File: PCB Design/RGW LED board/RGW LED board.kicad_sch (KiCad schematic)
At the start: 13 parts

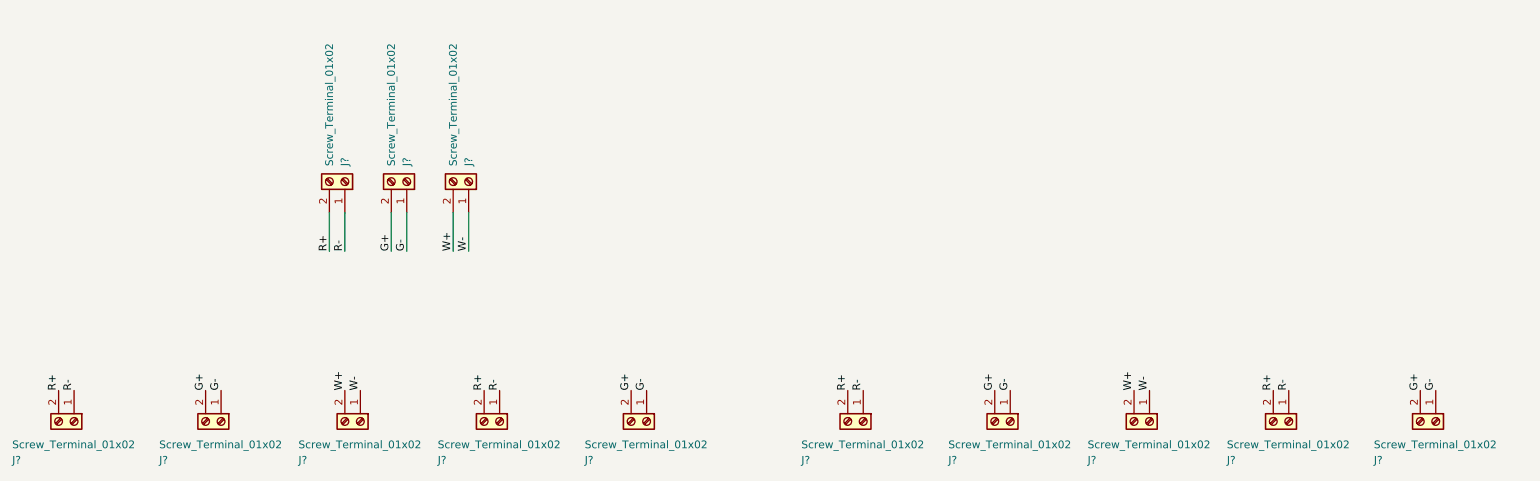
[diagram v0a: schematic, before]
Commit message: schematic now has no errors
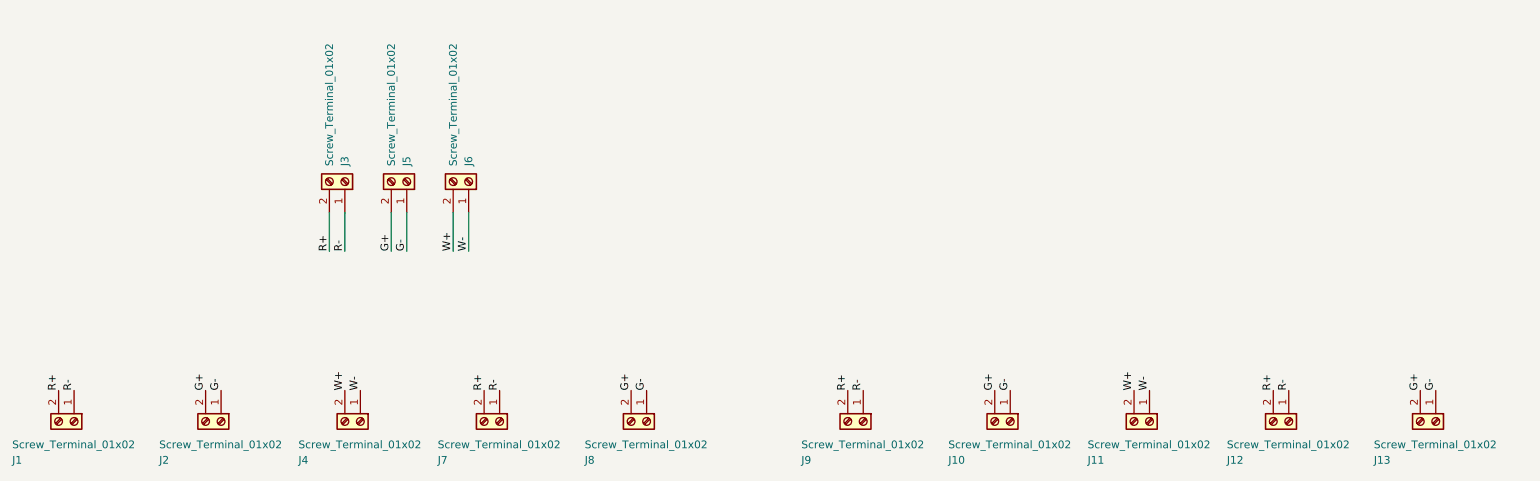
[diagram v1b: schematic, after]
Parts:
- gave numbers to parts that had none: 13
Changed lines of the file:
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@@
   (symbol (lib_id "Connector:Screw_Terminal_01x02") (at 69.85 100.33 270) (unit 1)
     (in_bom yes) (on_board yes)
-    (property "Reference" "J?" (id 0) (at 59.69 106.68 90)
+    (property "Reference" "J2" (id 0) (at 59.69 106.68 90)
       (effects (font (size 1.27 1.27)) (justify left))
     )
@@
   (symbol (lib_id "Connector:Screw_Terminal_01x02") (at 90.17 60.96 270) (mirror x) (unit 1)
     (in_bom yes) (on_board yes) (fields_autoplaced)
-    (property "Reference" "J?" (id 0) (at 90.1701 58.42 0)
+    (property "Reference" "J3" (id 0) (at 90.1701 58.42 0)
       (effects (font (size 1.27 1.27)) (justify left))
     )
@@
   (symbol (lib_id "Connector:Screw_Terminal_01x02") (at 245.11 100.33 270) (unit 1)
     (in_bom yes) (on_board yes)
-    (property "Reference" "J?" (id 0) (at 234.95 106.68 90)
+    (property "Reference" "J12" (id 0) (at 234.95 106.68 90)
       (effects (font (size 1.27 1.27)) (justify left))
     )
@@
   (symbol (lib_id "Connector:Screw_Terminal_01x02") (at 199.39 100.33 270) (unit 1)
     (in_bom yes) (on_board yes)
-    (property "Reference" "J?" (id 0) (at 189.23 106.68 90)
+    (property "Reference" "J10" (id 0) (at 189.23 106.68 90)
       (effects (font (size 1.27 1.27)) (justify left))
     )
@@
   (symbol (lib_id "Connector:Screw_Terminal_01x02") (at 45.72 100.33 270) (unit 1)
     (in_bom yes) (on_board yes)
-    (property "Reference" "J?" (id 0) (at 35.56 106.68 90)
+    (property "Reference" "J1" (id 0) (at 35.56 106.68 90)
       (effects (font (size 1.27 1.27)) (justify left))
     )
@@
   (symbol (lib_id "Connector:Screw_Terminal_01x02") (at 222.25 100.33 270) (unit 1)
     (in_bom yes) (on_board yes)
-    (property "Reference" "J?" (id 0) (at 212.09 106.68 90)
+    (property "Reference" "J11" (id 0) (at 212.09 106.68 90)
       (effects (font (size 1.27 1.27)) (justify left))
     )
@@
   (symbol (lib_id "Connector:Screw_Terminal_01x02") (at 115.57 100.33 270) (unit 1)
     (in_bom yes) (on_board yes)
-    (property "Reference" "J?" (id 0) (at 105.41 106.68 90)
+    (property "Reference" "J7" (id 0) (at 105.41 106.68 90)
       (effects (font (size 1.27 1.27)) (justify left))
     )
@@
   (symbol (lib_id "Connector:Screw_Terminal_01x02") (at 139.7 100.33 270) (unit 1)
     (in_bom yes) (on_board yes)
-    (property "Reference" "J?" (id 0) (at 129.54 106.68 90)
+    (property "Reference" "J8" (id 0) (at 129.54 106.68 90)
       (effects (font (size 1.27 1.27)) (justify left))
     )
@@
   (symbol (lib_id "Connector:Screw_Terminal_01x02") (at 100.33 60.96 270) (mirror x) (unit 1)
     (in_bom yes) (on_board yes) (fields_autoplaced)
-    (property "Reference" "J?" (id 0) (at 100.3301 58.42 0)
+    (property "Reference" "J5" (id 0) (at 100.3301 58.42 0)
       (effects (font (size 1.27 1.27)) (justify left))
     )
@@
   (symbol (lib_id "Connector:Screw_Terminal_01x02") (at 110.49 60.96 270) (mirror x) (unit 1)
     (in_bom yes) (on_board yes) (fields_autoplaced)
-    (property "Reference" "J?" (id 0) (at 110.4901 58.42 0)
+    (property "Reference" "J6" (id 0) (at 110.4901 58.42 0)
       (effects (font (size 1.27 1.27)) (justify left))
     )
@@
   (symbol (lib_id "Connector:Screw_Terminal_01x02") (at 175.26 100.33 270) (unit 1)
     (in_bom yes) (on_board yes)
-    (property "Reference" "J?" (id 0) (at 165.1 106.68 90)
+    (property "Reference" "J9" (id 0) (at 165.1 106.68 90)
       (effects (font (size 1.27 1.27)) (justify left))
     )
@@
   (symbol (lib_id "Connector:Screw_Terminal_01x02") (at 92.71 100.33 270) (unit 1)
     (in_bom yes) (on_board yes)
-    (property "Reference" "J?" (id 0) (at 82.55 106.68 90)
+    (property "Reference" "J4" (id 0) (at 82.55 106.68 90)
       (effects (font (size 1.27 1.27)) (justify left))
     )
@@
   (symbol (lib_id "Connector:Screw_Terminal_01x02") (at 269.24 100.33 270) (unit 1)
     (in_bom yes) (on_board yes)
-    (property "Reference" "J?" (id 0) (at 259.08 106.68 90)
+    (property "Reference" "J13" (id 0) (at 259.08 106.68 90)
       (effects (font (size 1.27 1.27)) (justify left))
     )
@@
   )
   (symbol_instances
+    (path "/59271f0a-9961-4fdc-9254-d35e340b8844"
+      (reference "J1") (unit 1) (value "Screw_Terminal_01x02") (footprint "Connector_PinHeader_2.54mm:PinHeader_1x02_P2.54mm_Vertical")
+    )
     (path "/05bc4c2d-ee3e-4b27-9ca2-add16f2c2396"
-      (reference "J?") (unit 1) (value "Screw_Terminal_01x02") (footprint "Connector_PinHeader_2.54mm:PinHeader_1x02_P2.54mm_Vertical")
+      (reference "J2") (unit 1) (value "Screw_Terminal_01x02") (footprint "Connector_PinHeader_2.54mm:PinHeader_1x02_P2.54mm_Vertical")
     )
     (path "/1e7cae58-6b42-419f-a0ef-656c9ebb3a41"
-      (reference "J?") (unit 1) (value "Screw_Terminal_01x02") (footprint "Connector_PinHeader_2.54mm:PinHeader_1x02_P2.54mm_Vertical")
+      (reference "J3") (unit 1) (value "Screw_Terminal_01x02") (footprint "Connector_PinHeader_2.54mm:PinHeader_1x02_P2.54mm_Vertical")
+    )
+    (path "/cdef1967-1f55-4bfe-8dbe-29150df572c3"
+      (reference "J4") (unit 1) (value "Screw_Terminal_01x02") (footprint "Connector_PinHeader_2.54mm:PinHeader_1x02_P2.54mm_Vertical")
+    )
+    (path "/7cca2ccf-cb11-4d5d-9ced-7f6969303b76"
+      (reference "J5") (unit 1) (value "Screw_Terminal_01x02") (footprint "Connector_PinHeader_2.54mm:PinHeader_1x02_P2.54mm_Vertical")
+    )
+    (path "/88f10c66-dda7-46b8-8caf-c98ed0e09c27"
+      (reference "J6") (unit 1) (value "Screw_Terminal_01x02") (footprint "Connector_PinHeader_2.54mm:PinHeader_1x02_P2.54mm_Vertical")
+    )
+    (path "/7aedd637-1cd8-47fd-b299-724180e1fa7b"
+      (reference "J7") (unit 1) (value "Screw_Terminal_01x02") (footprint "Connector_PinHeader_2.54mm:PinHeader_1x02_P2.54mm_Vertical")
+    )
+    (path "/7b3a097c-f841-4a54-8583-32e579f4440f"
+      (reference "J8") (unit 1) (value "Screw_Terminal_01x02") (footprint "Connector_PinHeader_2.54mm:PinHeader_1x02_P2.54mm_Vertical")
+    )
+    (path "/c30a76a9-64f5-4b01-80cf-8af90fc9d1c9"
+      (reference "J9") (unit 1) (value "Screw_Terminal_01x02") (footprint "Connector_PinHeader_2.54mm:PinHeader_1x02_P2.54mm_Vertical")
+    )
+    (path "/2282b147-a81b-4f06-be53-0e383bde0a1a"
+      (reference "J10") (unit 1) (value "Screw_Terminal_01x02") (footprint "Connector_PinHeader_2.54mm:PinHeader_1x02_P2.54mm_Vertical")
+    )
+    (path "/606a80ab-4a3a-4302-a9dd-66db51becec5"
+      (reference "J11") (unit 1) (value "Screw_Terminal_01x02") (footprint "Connector_PinHeader_2.54mm:PinHeader_1x02_P2.54mm_Vertical")
     )
     (path "/205c93a4-41c9-43d8-8f82-bdc6bf726d28"
-      (reference "J?") (unit 1) (value "Screw_Terminal_01x02") (footprint "Connector_PinHeader_2.54mm:PinHeader_1x02_P2.54mm_Vertical")
-    )
-    (path "/2282b147-a81b-4f06-be53-0e383bde0a1a"
-      (reference "J?") (unit 1) (value "Screw_Terminal_01x02") (footprint "Connector_PinHeader_2.54mm:PinHeader_1x02_P2.54mm_Vertical")
-    )
-    (path "/59271f0a-9961-4fdc-9254-d35e340b8844"
-      (reference "J?") (unit 1) (value "Screw_Terminal_01x02") (footprint "Connector_PinHeader_2.54mm:PinHeader_1x02_P2.54mm_Vertical")
-    )
-    (path "/606a80ab-4a3a-4302-a9dd-66db51becec5"
-      (reference "J?") (unit 1) (value "Screw_Terminal_01x02") (footprint "Connector_PinHeader_2.54mm:PinHeader_1x02_P2.54mm_Vertical")
-    )
-    (path "/7aedd637-1cd8-47fd-b299-724180e1fa7b"
-      (reference "J?") (unit 1) (value "Screw_Terminal_01x02") (footprint "Connector_PinHeader_2.54mm:PinHeader_1x02_P2.54mm_Vertical")
-    )
-    (path "/7b3a097c-f841-4a54-8583-32e579f4440f"
-      (reference "J?") (unit 1) (value "Screw_Terminal_01x02") (footprint "Connector_PinHeader_2.54mm:PinHeader_1x02_P2.54mm_Vertical")
-    )
-    (path "/7cca2ccf-cb11-4d5d-9ced-7f6969303b76"
-      (reference "J?") (unit 1) (value "Screw_Terminal_01x02") (footprint "Connector_PinHeader_2.54mm:PinHeader_1x02_P2.54mm_Vertical")
-    )
-    (path "/88f10c66-dda7-46b8-8caf-c98ed0e09c27"
-      (reference "J?") (unit 1) (value "Screw_Terminal_01x02") (footprint "Connector_PinHeader_2.54mm:PinHeader_1x02_P2.54mm_Vertical")
-    )
-    (path "/c30a76a9-64f5-4b01-80cf-8af90fc9d1c9"
-      (reference "J?") (unit 1) (value "Screw_Terminal_01x02") (footprint "Connector_PinHeader_2.54mm:PinHeader_1x02_P2.54mm_Vertical")
-    )
-    (path "/cdef1967-1f55-4bfe-8dbe-29150df572c3"
-      (reference "J?") (unit 1) (value "Screw_Terminal_01x02") (footprint "Connector_PinHeader_2.54mm:PinHeader_1x02_P2.54mm_Vertical")
+      (reference "J12") (unit 1) (value "Screw_Terminal_01x02") (footprint "Connector_PinHeader_2.54mm:PinHeader_1x02_P2.54mm_Vertical")
     )
     (path "/e67ce681-360e-4525-b138-4a854df1c513"
-      (reference "J?") (unit 1) (value "Screw_Terminal_01x02") (footprint "Connector_PinHeader_2.54mm:PinHeader_1x02_P2.54mm_Vertical")
-    )
-  )
+      (reference "J13") (unit 1) (value "Screw_Terminal_01x02") (footprint "Connector_PinHeader_2.54mm:PinHeader_1x02_P2.54mm_Vertical")
+    )
+  )

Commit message: Labeling on components
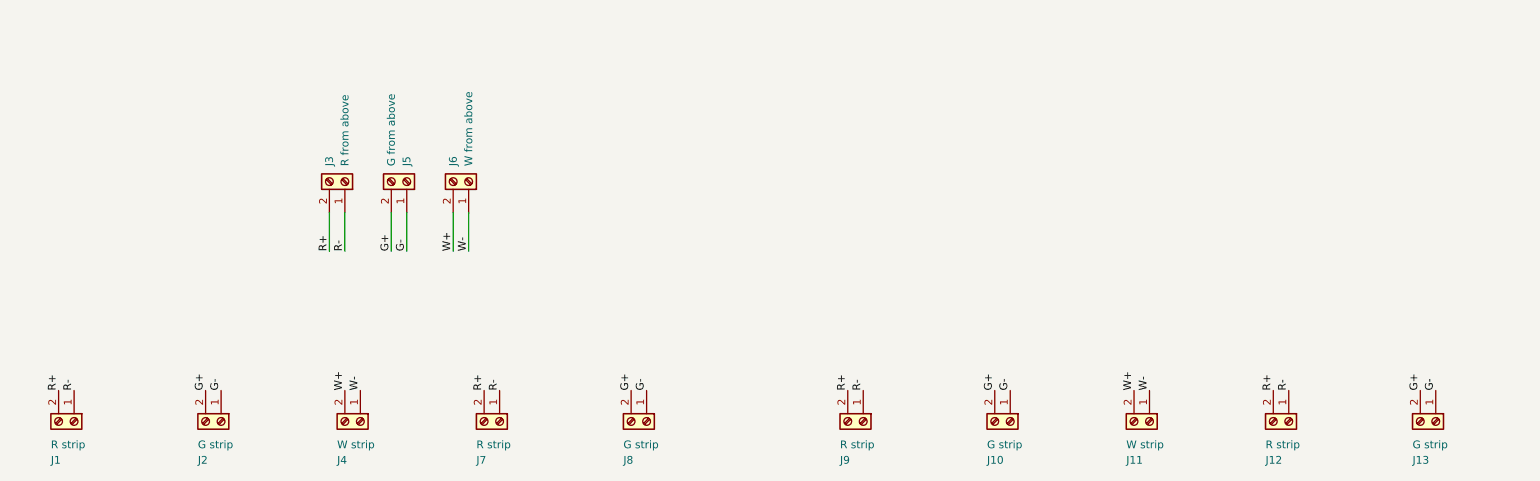
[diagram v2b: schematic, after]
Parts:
- J1, J12, J7, J9: value Screw_Terminal_01x02 -> R strip
- J10, J13, J2, J8: value Screw_Terminal_01x02 -> G strip
- J11, J4: value Screw_Terminal_01x02 -> W strip
- J3: value Screw_Terminal_01x02 -> R from above
- J5: value Screw_Terminal_01x02 -> G from above
- J6: value Screw_Terminal_01x02 -> W from above

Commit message: V2 IR and RGW boards done
Main board missing button footprint
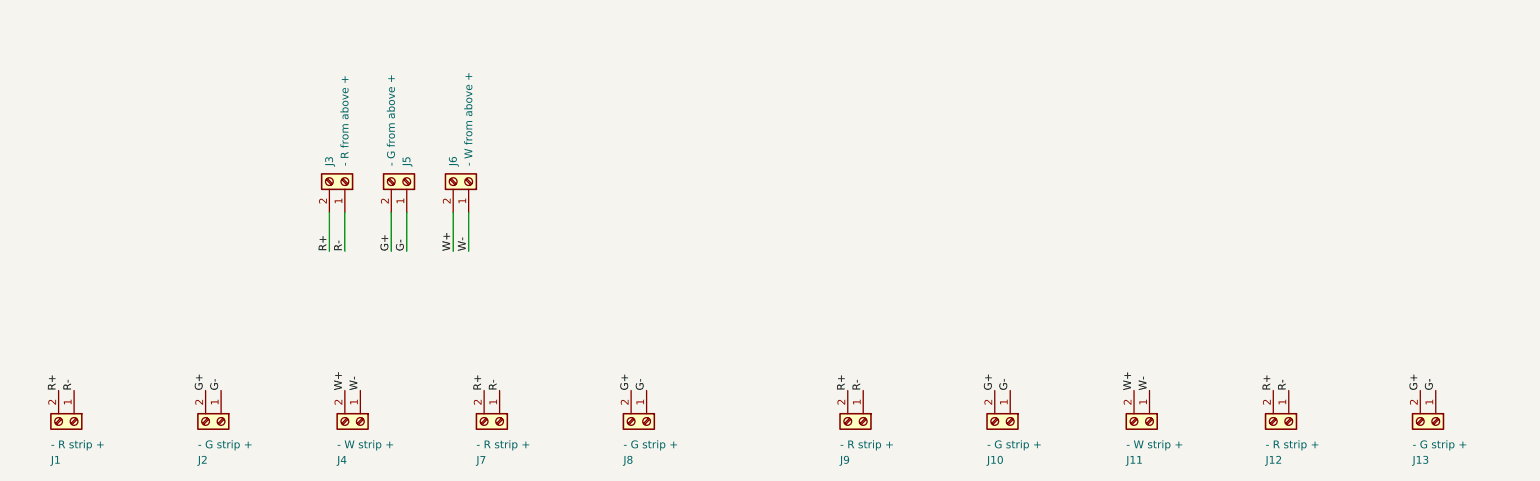
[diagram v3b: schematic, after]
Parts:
- J1, J12, J7, J9: value R strip -> - R strip +; footprint Connector_PinHeader_2.54mm:PinHeader_1x02_P2.54mm_Vertical -> TerminalBlock:TerminalBlock_bornier-2_P5.08mm
- J10, J13, J2, J8: value G strip -> - G strip +; footprint Connector_PinHeader_2.54mm:PinHeader_1x02_P2.54mm_Vertical -> TerminalBlock:TerminalBlock_bornier-2_P5.08mm
- J11, J4: value W strip -> - W strip +; footprint Connector_PinHeader_2.54mm:PinHeader_1x02_P2.54mm_Vertical -> TerminalBlock:TerminalBlock_bornier-2_P5.08mm
- J3: value R from above -> - R from above +; footprint Connector_PinHeader_2.54mm:PinHeader_1x02_P2.54mm_Vertical -> TerminalBlock:TerminalBlock_bornier-2_P5.08mm
- J5: value G from above -> - G from above +; footprint Connector_PinHeader_2.54mm:PinHeader_1x02_P2.54mm_Vertical -> TerminalBlock:TerminalBlock_bornier-2_P5.08mm
- J6: value W from above -> - W from above +; footprint Connector_PinHeader_2.54mm:PinHeader_1x02_P2.54mm_Vertical -> TerminalBlock:TerminalBlock_bornier-2_P5.08mm
